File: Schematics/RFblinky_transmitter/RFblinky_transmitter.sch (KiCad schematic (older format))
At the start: 7 parts, among them U1 LD1117S33TR_SOT223, U2 MSP430G2231IN14, U3 SMAKN-433TX

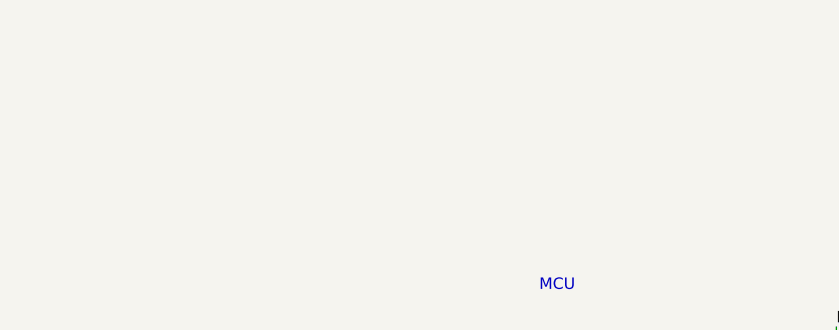
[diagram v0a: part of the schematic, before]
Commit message: Created schematic pdfs, added README, commented ReceiverModule
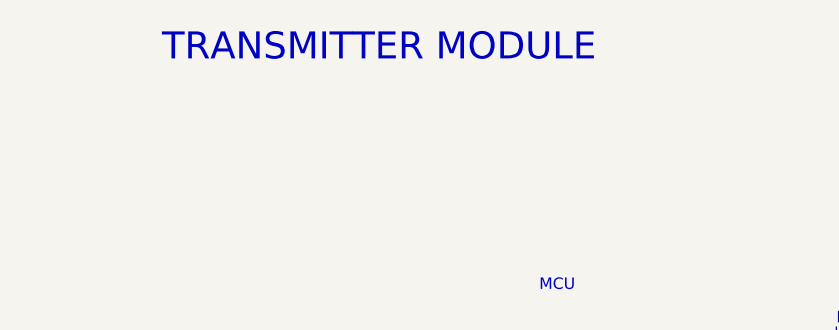
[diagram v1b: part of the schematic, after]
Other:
- note added: "TRANSMITTER MODULE"
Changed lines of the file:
@@
 Text Notes 10600 7650 0    50   ~ 0
 1.0\n
+Text Notes 4800 950  0    118  ~ 0
+TRANSMITTER MODULE
 $EndSCHEMATC
